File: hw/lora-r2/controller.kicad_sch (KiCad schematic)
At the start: 4 parts, among them J1 Conn_Coaxial, J2 SWD, U1 Pico_1_PCB

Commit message: First layout that passes DRC
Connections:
- net RADIO_BUSY: now also U1.22 (GPIO17); no longer U1.24 (GPIO18)
- net RADIO_INT: now also U1.21 (GPIO16); no longer U1.25 (GPIO19)
- net RADIO_RFSW_V1: now also U1.25 (GPIO19); no longer U1.22 (GPIO17)
- net RADIO_RFSW_V2: now also U1.24 (GPIO18); no longer U1.21 (GPIO16)
- net ANT: now reaches J1.1 (In), U2.12 (ANT_PAD)
- no-connect marks 10 -> 11

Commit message: Generated first Gerbers
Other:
- company: (none) -> Bruce MacKinnon
- title: (none) -> KC1FSZ LoRa Controller Board
- moved on the sheet: J1, U2

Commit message: SENT TO FAB (2025-05-08 13:04)
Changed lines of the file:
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@@
 	(text_box "Regarding AGND: \"If the ADC is not used or ADC performance is not critical, this pin can be connected to digital\nground.\""
 		(exclude_from_sim no)
-		(at 186.69 93.98 0)
-		(size 43.18 39.37)
+		(at 139.7 91.44 0)
+		(size 43.18 10.16)
 		(margins 0.9525 0.9525 0.9525 0.9525)
 		(stroke

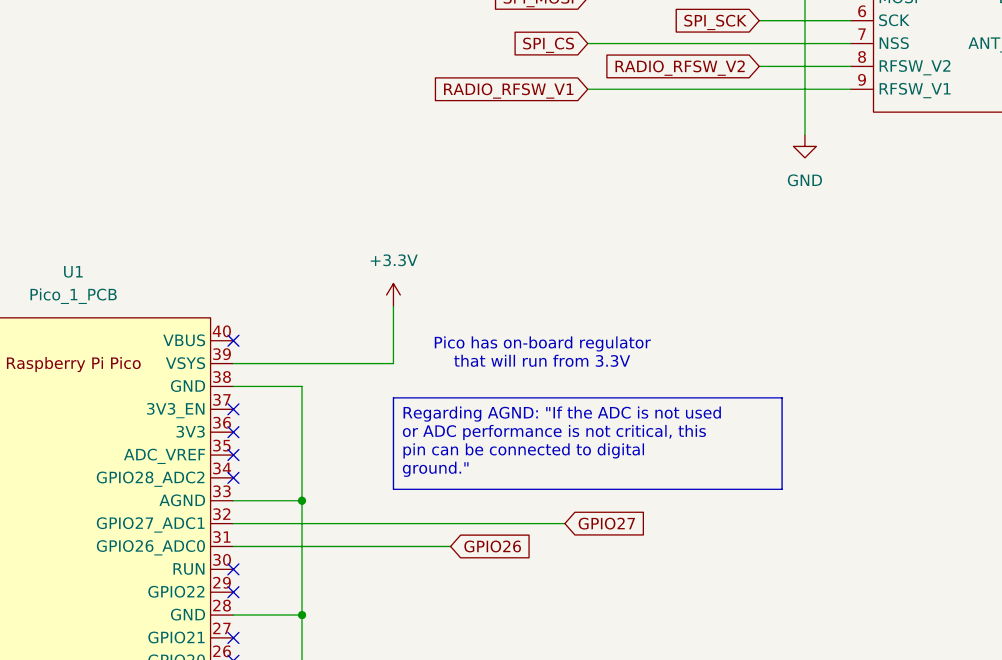
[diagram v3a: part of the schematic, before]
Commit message: Revision (before fab) - can power radio from USB now
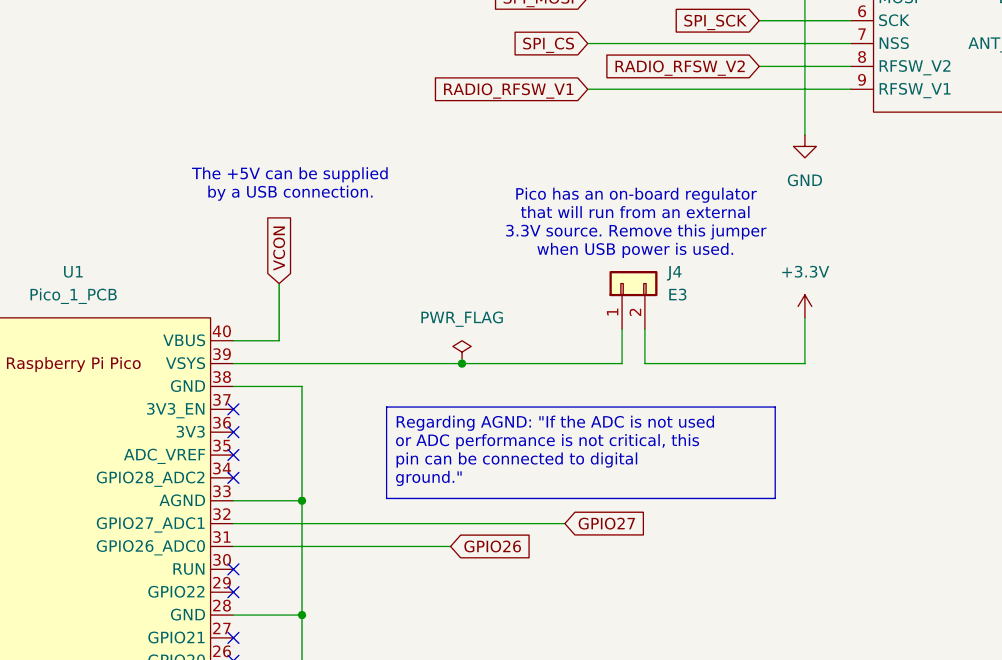
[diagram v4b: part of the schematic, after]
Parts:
- added J4: E3, Connector_PinHeader_2.54mm:PinHeader_1x02_P2.54mm_Vertical, symbol Connector_Generic:Conn_01x02
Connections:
- net +3.3V: now also J4.2 (Pin_2); no longer U1.39 (VSYS)
- net VCON: now reaches U1.40 (VBUS)
- new net: J4.1 (Pin_1), U1.39 (VSYS)
- no-connect marks 11 -> 10
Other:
- note added: "Pico has an on-board regulator that will run from an external 3.3V source. Remove this jumper when USB power is used."
- note added: "The +5V can be supplied by a USB connection."
- note removed: "Pico has on-board regulator that will run from 3.3V"
